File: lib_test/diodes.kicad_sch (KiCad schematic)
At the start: 1 part

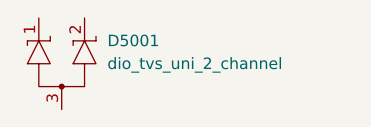
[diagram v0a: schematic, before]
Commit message: add diode SS14
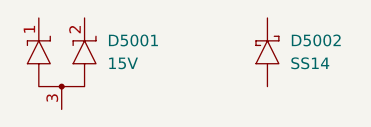
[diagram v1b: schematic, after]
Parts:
- added D5002: SS14, lily_footprints:dio_do214ac_sma, symbol lily_symbols:dio_schottky_SS14_do214ac_sma
- D5001: value dio_tvs_uni_2_channel -> 15V
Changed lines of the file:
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@@
+	)
+	(symbol
+		(lib_id "lily_symbols:dio_schottky_SS14_do214ac_sma")
+		(at 50.8 25.4 0)
+		(unit 1)
+		(exclude_from_sim no)
+		(in_bom yes)
+		(on_board yes)
+		(dnp no)
+		(property "Reference" "D5002"
+			(at 53.34 27.94 0)
+			(effects
+				(font
+					(size 1.27 1.27)
+				)
+				(justify left)
+			)
+		)
+		(property "Value" "SS14"
+			(at 53.34 30.48 0)
+			(effects
+				(font
+					(size 1.27 1.27)
+				)
+				(justify left)
+			)
+		)
+		(property "Footprint" "lily_footprints:dio_do214ac_sma"
+			(at 50.8 45.72 0)
+			(effects
+				(font
+					(size 1.27 1.27)
+				)
+				(hide yes)
+			)
+		)
+		(property "Datasheet" ""
+			(at 50.8 33.02 90)
+			(effects
+				(font
+					(size 1.27 1.27)
+				)
+				(hide yes)
+			)
+		)
+		(property "Description" ""
+			(at 50.8 25.4 0)
+			(effects
+				(font
+					(size 1.27 1.27)
+				)
+				(hide yes)
+			)
+		)
+		(property "Revision" "1"
+			(at 50.8 40.64 0)
+			(effects
+				(font
+					(size 1.27 1.27)
+				)
+				(hide yes)
+			)
+		)
+		(property "Status" "Active"
+			(at 50.8 43.18 0)
+			(effects
+				(font
+					(size 1.27 1.27)
+				)
+				(hide yes)
+			)
+		)
+		(property "Manufacturer" "Microdiode Electronics"
+			(at 50.8 48.26 0)
+			(effects
+				(font
+					(size 1.27 1.27)
+				)
+				(hide yes)
+			)
+		)
+		(property "Manufacturer_ID" "SS14"
+			(at 50.8 50.8 0)
+			(effects
+				(font
+					(size 1.27 1.27)
+				)
+				(hide yes)
+			)
+		)
+		(property "Lily_ID" "1911-10002"
+			(at 50.8 53.34 0)
+			(effects
+				(font
+					(size 1.27 1.27)
+				)
+				(hide yes)
+			)
+		)
+		(property "JLCPCB_ID" "C2480"
+			(at 50.8 55.88 0)
+			(effects
+				(font
+					(size 1.27 1.27)
+				)
+				(hide yes)
+			)
+		)
+		(property "JLCPCB_STATUS" "Basic"
+			(at 50.8 58.42 0)
+			(effects
+				(font
+					(size 1.27 1.27)
+				)
+				(hide yes)
+			)
+		)
+		(pin "2"
+		)
+		(pin "1"
+		)
+		(instances
+			(project "kicad_lib_test"
+				(path "/032b8f2d-5c08-4381-9e3a-c197ca84e3c5/f8e61c5d-b401-4177-96aa-be2ecb8375a7"
+					(reference "D5002")
+					(unit 1)
+				)
+			)
+		)
 	)
 	(symbol
@@
 			)
 		)
-		(property "Value" "dio_tvs_uni_2_channel"
+		(property "Value" "15V"
 			(at 33.02 30.48 0)
 			(effects

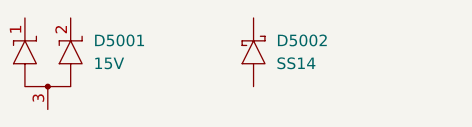
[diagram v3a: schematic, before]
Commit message: add TVS 15V
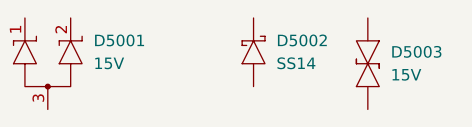
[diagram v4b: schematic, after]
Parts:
- added D5003: 15V, lily_footprints:dio_do214aa_smb, symbol lily_symbols:dio_tvs_bidi_15V_smb
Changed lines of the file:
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@@
+		)
+	)
+	(symbol
+		(lib_id "lily_symbols:dio_tvs_bidi_15V_smb")
+		(at 63.5 25.4 0)
+		(unit 1)
+		(exclude_from_sim no)
+		(in_bom yes)
+		(on_board yes)
+		(dnp no)
+		(property "Reference" "D5003"
+			(at 66.04 29.21 0)
+			(effects
+				(font
+					(size 1.27 1.27)
+				)
+				(justify left)
+			)
+		)
+		(property "Value" "15V"
+			(at 66.04 31.75 0)
+			(effects
+				(font
+					(size 1.27 1.27)
+				)
+				(justify left)
+			)
+		)
+		(property "Footprint" "lily_footprints:dio_do214aa_smb"
+			(at 63.5 48.26 0)
+			(effects
+				(font
+					(size 1.27 1.27)
+				)
+				(hide yes)
+			)
+		)
+		(property "Datasheet" ""
+			(at 63.5 35.56 90)
+			(effects
+				(font
+					(size 1.27 1.27)
+				)
+				(hide yes)
+			)
+		)
+		(property "Description" ""
+			(at 63.5 25.4 0)
+			(effects
+				(font
+					(size 1.27 1.27)
+				)
+				(hide yes)
+			)
+		)
+		(property "Revision" "1"
+			(at 63.5 43.18 0)
+			(effects
+				(font
+					(size 1.27 1.27)
+				)
+				(hide yes)
+			)
+		)
+		(property "Status" "Active"
+			(at 63.5 45.72 0)
+			(effects
+				(font
+					(size 1.27 1.27)
+				)
+				(hide yes)
+			)
+		)
+		(property "Manufacturer" "Hongjiacheng"
+			(at 63.5 50.8 0)
+			(effects
+				(font
+					(size 1.27 1.27)
+				)
+				(hide yes)
+			)
+		)
+		(property "Manufacturer_ID" "SMBJ15CA"
+			(at 63.5 53.34 0)
+			(effects
+				(font
+					(size 1.27 1.27)
+				)
+				(hide yes)
+			)
+		)
+		(property "Lily_ID" "1911-10004"
+			(at 63.5 55.88 0)
+			(effects
+				(font
+					(size 1.27 1.27)
+				)
+				(hide yes)
+			)
+		)
+		(property "JLCPCB_ID" "C19077570"
+			(at 63.5 58.42 0)
+			(effects
+				(font
+					(size 1.27 1.27)
+				)
+				(hide yes)
+			)
+		)
+		(property "JLCPCB_STATUS" "Extended preferred"
+			(at 63.5 60.96 0)
+			(effects
+				(font
+					(size 1.27 1.27)
+				)
+				(hide yes)
+			)
+		)
+		(pin "1"
+		)
+		(pin "2"
+		)
+		(instances
+			(project "kicad_lib_test"
+				(path "/032b8f2d-5c08-4381-9e3a-c197ca84e3c5/f8e61c5d-b401-4177-96aa-be2ecb8375a7"
+					(reference "D5003")
+					(unit 1)
+				)
+			)
 		)
 	)

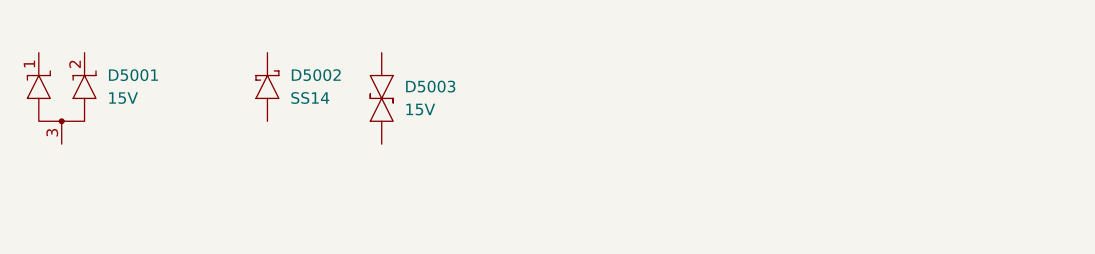
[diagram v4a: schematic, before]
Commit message: add diode TVS 4 channel 5V
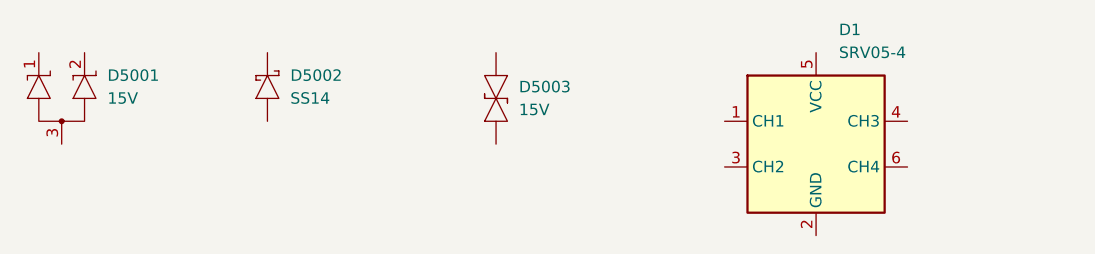
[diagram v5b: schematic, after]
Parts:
- added D1: SRV05-4, lily_footprints:sot23-6_sc74, symbol lily_symbols:dio_tvs_uni_4_channel_5V_SRV05-4_sot23-6
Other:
- moved on the sheet: D5003
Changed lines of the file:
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@@
+	)
+	(symbol
+		(lib_id "lily_symbols:dio_tvs_uni_4_channel_5V_SRV05-4_sot23-6")
+		(at 101.6 33.02 0)
+		(unit 1)
+		(exclude_from_sim no)
+		(in_bom yes)
+		(on_board yes)
+		(dnp no)
+		(property "Reference" "D1"
+			(at 114.3 22.86 0)
+			(effects
+				(font
+					(size 1.27 1.27)
+				)
+				(justify left)
+			)
+		)
+		(property "Value" "SRV05-4"
+			(at 114.3 25.4 0)
+			(effects
+				(font
+					(size 1.27 1.27)
+				)
+				(justify left)
+			)
+		)
+		(property "Footprint" "lily_footprints:sot23-6_sc74"
+			(at 111.76 63.5 0)
+			(effects
+				(font
+					(size 1.27 1.27)
+				)
+				(hide yes)
+			)
+		)
+		(property "Datasheet" ""
+			(at 86.36 17.78 0)
+			(effects
+				(font
+					(size 1.27 1.27)
+				)
+				(hide yes)
+			)
+		)
+		(property "Description" ""
+			(at 101.6 33.02 0)
+			(effects
+				(font
+					(size 1.27 1.27)
+				)
+				(hide yes)
+			)
+		)
+		(property "Revision" "1"
+			(at 111.76 58.42 0)
+			(effects
+				(font
+					(size 1.27 1.27)
+				)
+				(hide yes)
+			)
+		)
+		(property "Status" "Active"
+			(at 111.76 60.96 0)
+			(effects
+				(font
+					(size 1.27 1.27)
+				)
+				(hide yes)
+			)
+		)
+		(property "Manufacturer" "Tech Public"
+			(at 111.76 66.04 0)
+			(effects
+				(font
+					(size 1.27 1.27)
+				)
+				(hide yes)
+			)
+		)
+		(property "Manufacturer_ID" "SRV05-4"
+			(at 111.76 68.58 0)
+			(effects
+				(font
+					(size 1.27 1.27)
+				)
+				(hide yes)
+			)
+		)
+		(property "Lily_ID" "1911-10006"
+			(at 111.76 71.12 0)
+			(effects
+				(font
+					(size 1.27 1.27)
+				)
+				(hide yes)
+			)
+		)
+		(property "JLCPCB_ID" "C558418"
+			(at 111.76 73.66 0)
+			(effects
+				(font
+					(size 1.27 1.27)
+				)
+				(hide yes)
+			)
+		)
+		(property "JLCPCB_STATUS" "Extended"
+			(at 111.76 76.2 0)
+			(effects
+				(font
+					(size 1.27 1.27)
+				)
+				(hide yes)
+			)
+		)
+		(pin "4"
+		)
+		(pin "1"
+		)
+		(pin "5"
+		)
+		(pin "6"
+		)
+		(pin "2"
+		)
+		(pin "3"
+		)
+		(instances
+			(project "kicad_lib_test"
+				(path "/032b8f2d-5c08-4381-9e3a-c197ca84e3c5/f8e61c5d-b401-4177-96aa-be2ecb8375a7"
+					(reference "D1")
+					(unit 1)
+				)
+			)
+		)
 	)
 	(symbol
@@
 	(symbol
 		(lib_id "lily_symbols:dio_tvs_bidi_15V_smb")
-		(at 63.5 25.4 0)
+		(at 76.2 25.4 0)
 		(unit 1)
 		(exclude_from_sim no)
@@
 		(dnp no)
 		(property "Reference" "D5003"
-			(at 66.04 29.21 0)
+			(at 78.74 29.21 0)
 			(effects
 				(font
@@
 		)
 		(property "Value" "15V"
-			(at 66.04 31.75 0)
+			(at 78.74 31.75 0)
 			(effects
 				(font
@@
 		)
 		(property "Footprint" "lily_footprints:dio_do214aa_smb"
-			(at 63.5 48.26 0)
+			(at 76.2 48.26 0)
 			(effects
 				(font
@@
 		)
 		(property "Datasheet" ""
-			(at 63.5 35.56 90)
+			(at 76.2 35.56 90)
 			(effects
 				(font
@@
 		)
 		(property "Description" ""
-			(at 63.5 25.4 0)
+			(at 76.2 25.4 0)
 			(effects
 				(font
@@
 		)
 		(property "Revision" "1"
-			(at 63.5 43.18 0)
+			(at 76.2 43.18 0)
 			(effects
 				(font
@@
 		)
 		(property "Status" "Active"
-			(at 63.5 45.72 0)
+			(at 76.2 45.72 0)
 			(effects
 				(font
@@
 		)
 		(property "Manufacturer" "Hongjiacheng"
-			(at 63.5 50.8 0)
+			(at 76.2 50.8 0)
 			(effects
 				(font
@@
 		)
 		(property "Manufacturer_ID" "SMBJ15CA"
-			(at 63.5 53.34 0)
+			(at 76.2 53.34 0)
 			(effects
 				(font
@@
 		)
 		(property "Lily_ID" "1911-10004"
-			(at 63.5 55.88 0)
+			(at 76.2 55.88 0)
 			(effects
 				(font
@@
 		)
 		(property "JLCPCB_ID" "C19077570"
-			(at 63.5 58.42 0)
+			(at 76.2 58.42 0)
 			(effects
 				(font
@@
 		)
 		(property "JLCPCB_STATUS" "Extended preferred"
-			(at 63.5 60.96 0)
-			(effects
-				(font
+			(at 76.2 60.96 0)
+			(effects
+				(font

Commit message: add diode zener 4V7
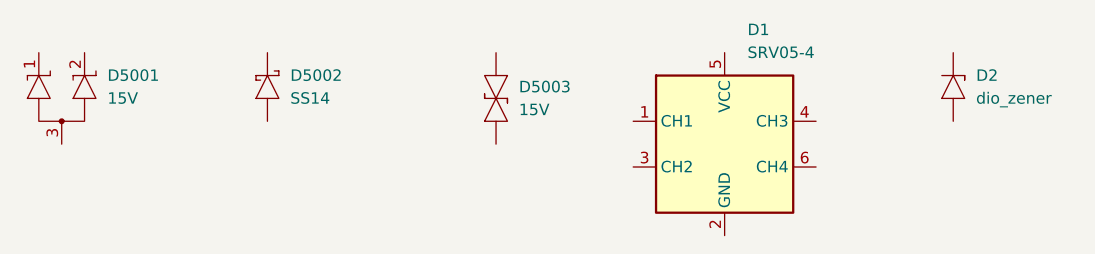
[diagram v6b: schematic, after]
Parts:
- added D2: dio_zener, lily_footprints:dio_sod323, symbol lily_symbols:dio_zener_4V7_200mW_SOD323
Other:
- moved on the sheet: D1
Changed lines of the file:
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@@
 	(symbol
 		(lib_id "lily_symbols:dio_tvs_uni_4_channel_5V_SRV05-4_sot23-6")
-		(at 101.6 33.02 0)
+		(at 91.44 33.02 0)
 		(unit 1)
 		(exclude_from_sim no)
@@
 		(dnp no)
 		(property "Reference" "D1"
-			(at 114.3 22.86 0)
+			(at 104.14 22.86 0)
 			(effects
 				(font
@@
 		)
 		(property "Value" "SRV05-4"
-			(at 114.3 25.4 0)
+			(at 104.14 25.4 0)
 			(effects
 				(font
@@
 		)
 		(property "Footprint" "lily_footprints:sot23-6_sc74"
-			(at 111.76 63.5 0)
+			(at 101.6 63.5 0)
 			(effects
 				(font
@@
 		)
 		(property "Datasheet" ""
-			(at 86.36 17.78 0)
+			(at 76.2 17.78 0)
 			(effects
 				(font
@@
 		)
 		(property "Description" ""
-			(at 101.6 33.02 0)
+			(at 91.44 33.02 0)
 			(effects
 				(font
@@
 		)
 		(property "Revision" "1"
-			(at 111.76 58.42 0)
+			(at 101.6 58.42 0)
 			(effects
 				(font
@@
 		)
 		(property "Status" "Active"
-			(at 111.76 60.96 0)
+			(at 101.6 60.96 0)
 			(effects
 				(font
@@
 		)
 		(property "Manufacturer" "Tech Public"
-			(at 111.76 66.04 0)
+			(at 101.6 66.04 0)
 			(effects
 				(font
@@
 		)
 		(property "Manufacturer_ID" "SRV05-4"
-			(at 111.76 68.58 0)
+			(at 101.6 68.58 0)
 			(effects
 				(font
@@
 		)
 		(property "Lily_ID" "1911-10006"
-			(at 111.76 71.12 0)
+			(at 101.6 71.12 0)
 			(effects
 				(font
@@
 		)
 		(property "JLCPCB_ID" "C558418"
-			(at 111.76 73.66 0)
+			(at 101.6 73.66 0)
 			(effects
 				(font
@@
 		)
 		(property "JLCPCB_STATUS" "Extended"
-			(at 111.76 76.2 0)
+			(at 101.6 76.2 0)
 			(effects
 				(font
@@
 					(unit 1)
 				)
+			)
+		)
+	)
+	(symbol
+		(lib_id "lily_symbols:dio_zener_4V7_200mW_SOD323")
+		(at 127 25.4 0)
+		(unit 1)
+		(exclude_from_sim no)
+		(in_bom yes)
+		(on_board yes)
+		(dnp no)
+		(property "Reference" "D2"
+			(at 129.54 27.94 0)
+			(effects
+				(font
+					(size 1.27 1.27)
+				)
+				(justify left)
+			)
+		)
+		(property "Value" "dio_zener"
+			(at 129.54 30.48 0)
+			(effects
+				(font
+					(size 1.27 1.27)
+				)
+				(justify left)
+			)
+		)
+		(property "Footprint" "lily_footprints:dio_sod323"
+			(at 127 45.72 0)
+			(effects
+				(font
+					(size 1.27 1.27)
+				)
+				(hide yes)
+			)
+		)
+		(property "Datasheet" ""
+			(at 127 33.02 90)
+			(effects
+				(font
+					(size 1.27 1.27)
+				)
+				(hide yes)
+			)
+		)
+		(property "Description" ""
+			(at 127 25.4 0)
+			(effects
+				(font
+					(size 1.27 1.27)
+				)
+				(hide yes)
+			)
+		)
+		(property "Revision" "1"
+			(at 127 40.64 0)
+			(effects
+				(font
+					(size 1.27 1.27)
+				)
+				(hide yes)
+			)
+		)
+		(property "Status" "Active"
+			(at 127 43.18 0)
+			(effects
+				(font
+					(size 1.27 1.27)
+				)
+				(hide yes)
+			)
+		)
+		(property "Manufacturer" "Guangdong Hottech"
+			(at 127 48.26 0)
+			(effects
+				(font
+					(size 1.27 1.27)
+				)
+				(hide yes)
+			)
+		)
+		(property "Manufacturer_ID" "BZT52C4V7S"
+			(at 127 50.8 0)
+			(effects
+				(font
+					(size 1.27 1.27)
+				)
+				(hide yes)
+			)
+		)
+		(property "Lily_ID" "1911-10005"
+			(at 127.635 53.34 0)
+			(effects
+				(font
+					(size 1.27 1.27)
+				)
+				(hide yes)
+			)
+		)
+		(property "JLCPCB_ID" "C5190168"
+			(at 127 55.88 0)
+			(effects
+				(font
+					(size 1.27 1.27)
+				)
+				(hide yes)
+			)
+		)
+		(property "JLCPCB_STATUS" "Extended"
+			(at 127 58.42 0)
+			(effects
+				(font
+					(size 1.27 1.27)
+				)
+				(hide yes)
+			)
+		)
+		(pin "1"
+		)
+		(pin "2"
+		)
+		(instances
+			(project "kicad_lib_test"
+				(path "/032b8f2d-5c08-4381-9e3a-c197ca84e3c5/f8e61c5d-b401-4177-96aa-be2ecb8375a7"
+					(reference "D2")
+					(unit 1)
+				)

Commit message: updated test design
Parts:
- renumbered D2 to D5004, D1 to D5005
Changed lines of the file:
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@@
 		(on_board yes)
 		(dnp no)
-		(property "Reference" "D1"
+		(property "Reference" "D5005"
 			(at 104.14 22.86 0)
 			(effects
@@
 			(project "kicad_lib_test"
 				(path "/032b8f2d-5c08-4381-9e3a-c197ca84e3c5/f8e61c5d-b401-4177-96aa-be2ecb8375a7"
-					(reference "D1")
+					(reference "D5005")
 					(unit 1)
 				)
@@
 		(on_board yes)
 		(dnp no)
-		(property "Reference" "D2"
+		(property "Reference" "D5004"
 			(at 129.54 27.94 0)
 			(effects
@@
 			(project "kicad_lib_test"
 				(path "/032b8f2d-5c08-4381-9e3a-c197ca84e3c5/f8e61c5d-b401-4177-96aa-be2ecb8375a7"
-					(reference "D2")
+					(reference "D5004")
 					(unit 1)
 				)

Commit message: fix symbol properties
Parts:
- D5005: JLCPCB_ID C558418 -> C85364; JLCPCB_STATUS Extended -> Extended Preferred; Manufacturer Tech Public -> ProTek Devices; Manufacturer_ID SRV05-4 -> SRV05-4-P-T7
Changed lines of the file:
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@@
 			)
 		)
-		(property "Manufacturer" "Tech Public"
+		(property "Manufacturer" "ProTek Devices"
 			(at 101.6 66.04 0)
 			(effects
@@
 			)
 		)
-		(property "Manufacturer_ID" "SRV05-4"
+		(property "Manufacturer_ID" "SRV05-4-P-T7"
 			(at 101.6 68.58 0)
 			(effects
@@
 			)
 		)
-		(property "JLCPCB_ID" "C558418"
+		(property "JLCPCB_ID" "C85364"
 			(at 101.6 73.66 0)
 			(effects
@@
 			)
 		)
-		(property "JLCPCB_STATUS" "Extended"
+		(property "JLCPCB_STATUS" "Extended Preferred"
 			(at 101.6 76.2 0)
 			(effects
